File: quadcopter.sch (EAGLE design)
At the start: 77 parts, among them J1 AVR_SPI_PRG_6NS, J3 HEADER-0.1IN-2POS-FEMALE, J4 HEADER-0.1IN-2POS-FEMALE, J5 HEADER-0.1IN-2POS-FEMALE, J6 HEADER-0.1IN-2POS-FEMALE, J8 HEADER-0.1IN-2POS-FEMALE, SW1 PUSHBUTTON_SMD-VERTICAL, SW2 PUSHBUTTON_SMD-VERTICAL, U1 ATMEGA128RFA1

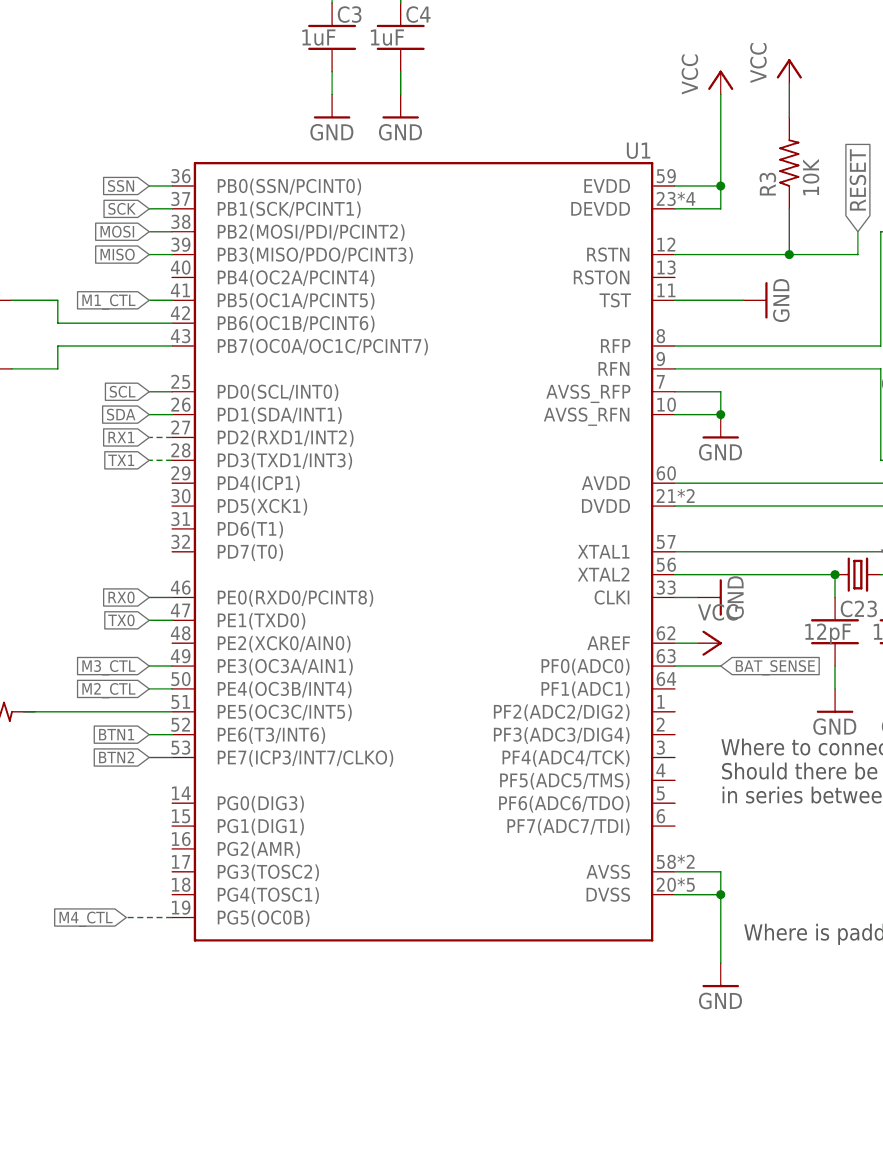
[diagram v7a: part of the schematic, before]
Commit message: More gnd cleaning
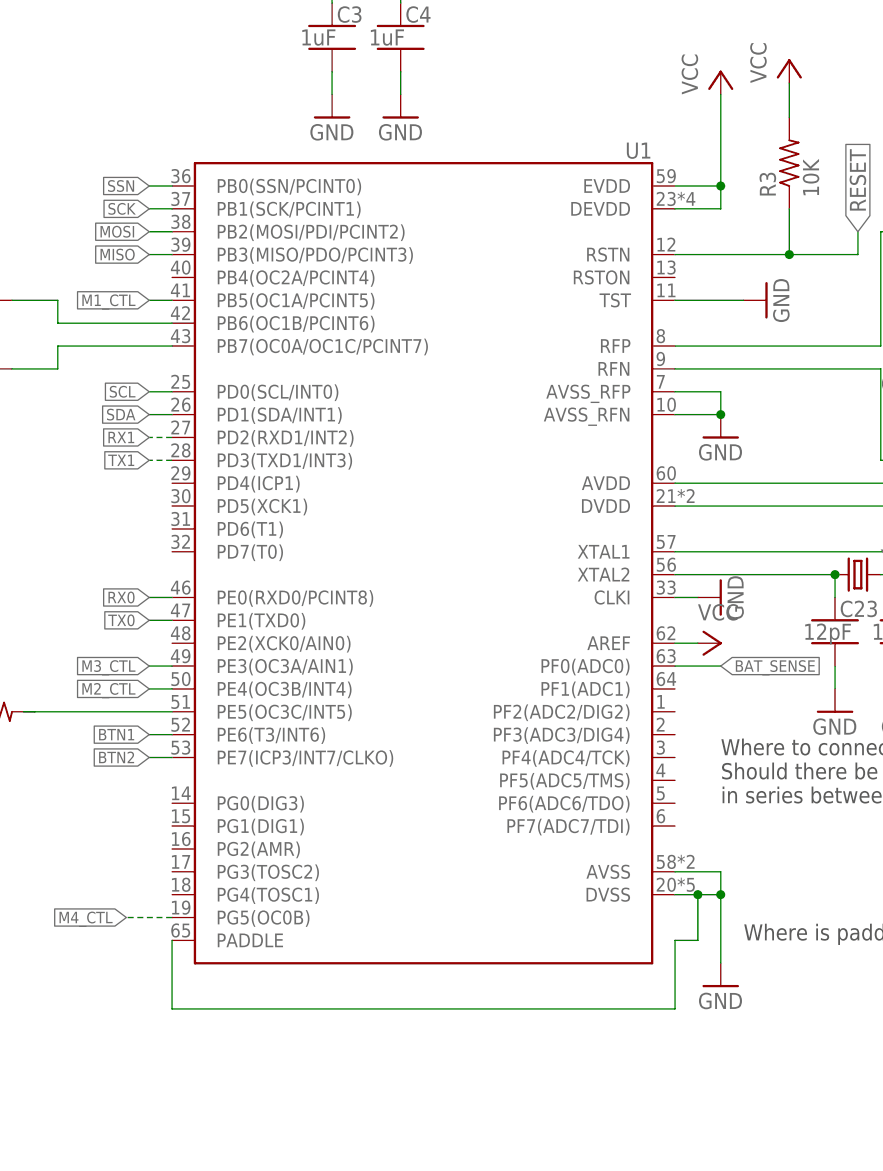
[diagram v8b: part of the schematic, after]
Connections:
- net GND: now also U1.PADDLE
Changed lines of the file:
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@@
 <wire x1="248.92" y1="-203.2" x2="248.92" y2="-195.58" width="0.1524" layer="91"/>
 <pinref part="U1" gate="G$1" pin="DVSS"/>
-<wire x1="243.84" y1="-195.58" x2="248.92" y2="-195.58" width="0.1524" layer="91"/>
+<wire x1="243.84" y1="-195.58" x2="246.38" y2="-195.58" width="0.1524" layer="91"/>
 <pinref part="U1" gate="G$1" pin="AVSS"/>
+<wire x1="246.38" y1="-195.58" x2="248.92" y2="-195.58" width="0.1524" layer="91"/>
 <wire x1="243.84" y1="-193.04" x2="248.92" y2="-193.04" width="0.1524" layer="91"/>
 <wire x1="248.92" y1="-193.04" x2="248.92" y2="-195.58" width="0.1524" layer="91"/>
 <junction x="248.92" y="-195.58"/>
+<pinref part="U1" gate="G$1" pin="PADDLE"/>
+<wire x1="187.96" y1="-200.66" x2="187.96" y2="-208.28" width="0.1524" layer="91"/>
+<wire x1="187.96" y1="-208.28" x2="243.84" y2="-208.28" width="0.1524" layer="91"/>
+<wire x1="243.84" y1="-208.28" x2="243.84" y2="-200.66" width="0.1524" layer="91"/>
+<wire x1="243.84" y1="-200.66" x2="246.38" y2="-200.66" width="0.1524" layer="91"/>
+<wire x1="246.38" y1="-200.66" x2="246.38" y2="-195.58" width="0.1524" layer="91"/>
+<junction x="246.38" y="-195.58"/>
 </segment>
 <segment>
